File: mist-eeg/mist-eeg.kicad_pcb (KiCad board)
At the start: 4 copper layers, 50 x 75 mm, 233 parts, among them J1 Power_5V-14V, J10 J1310, J3 Audio, J4 Electrodes, J5 Micro_SD_Card_Det, J6 Extra GPIOs, J7 Digital buses, J8 J1312, J9 J1311, Q1 NMOS_DGS (3V3), Q2 NMOS_DGS (3.3V), Q3 NMOS_DGS (3.3V), Q4 PMOS_DGS (3.3V @ 1A), SW1 START, SW2 USER, SW3 SD_RST, SW4 RESET, SW5 ONOFF, U1 LTC2947, U10 ADAU1372, U11 ADS1299, U12 NX5427001Z, U5 TPS63070, U6 LT3042xMSE, U7 LT3042xMSE, U8 TPS63070, U9 TPS63070

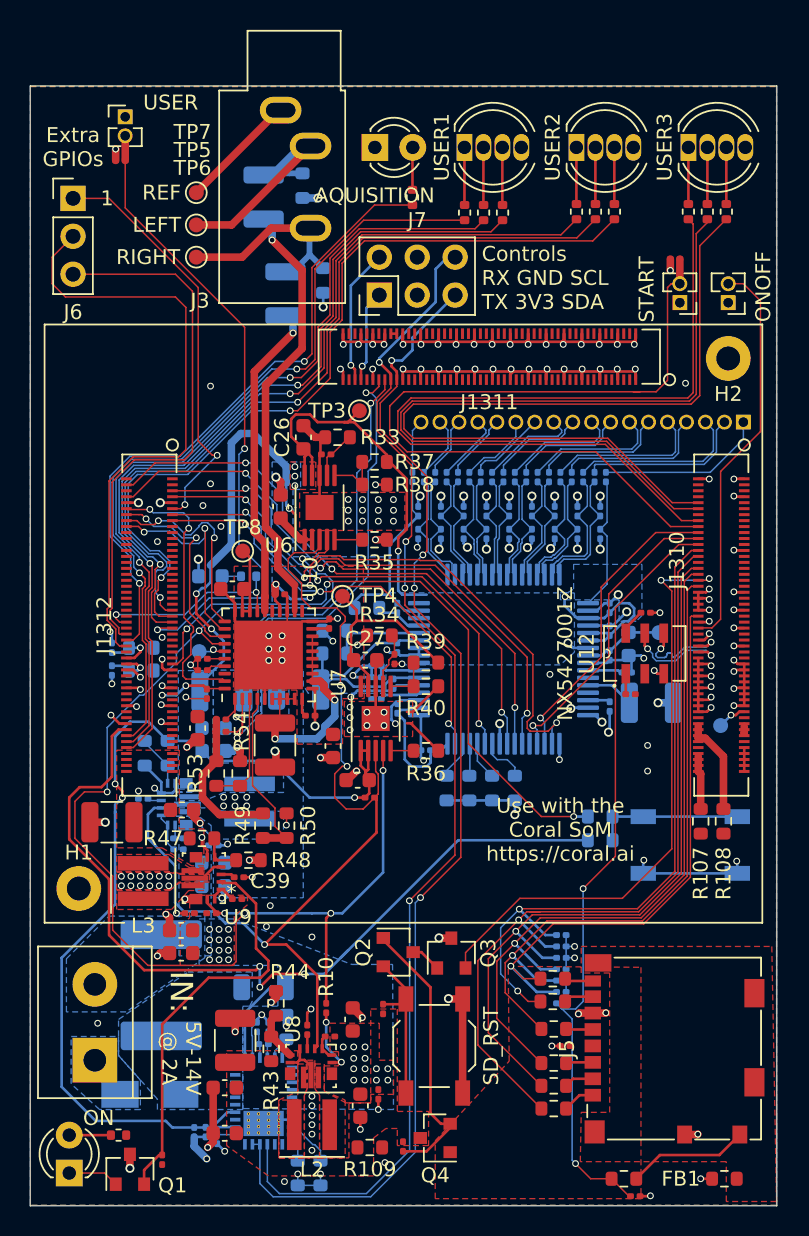
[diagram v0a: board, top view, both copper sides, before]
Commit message: Change buckboost regulator used
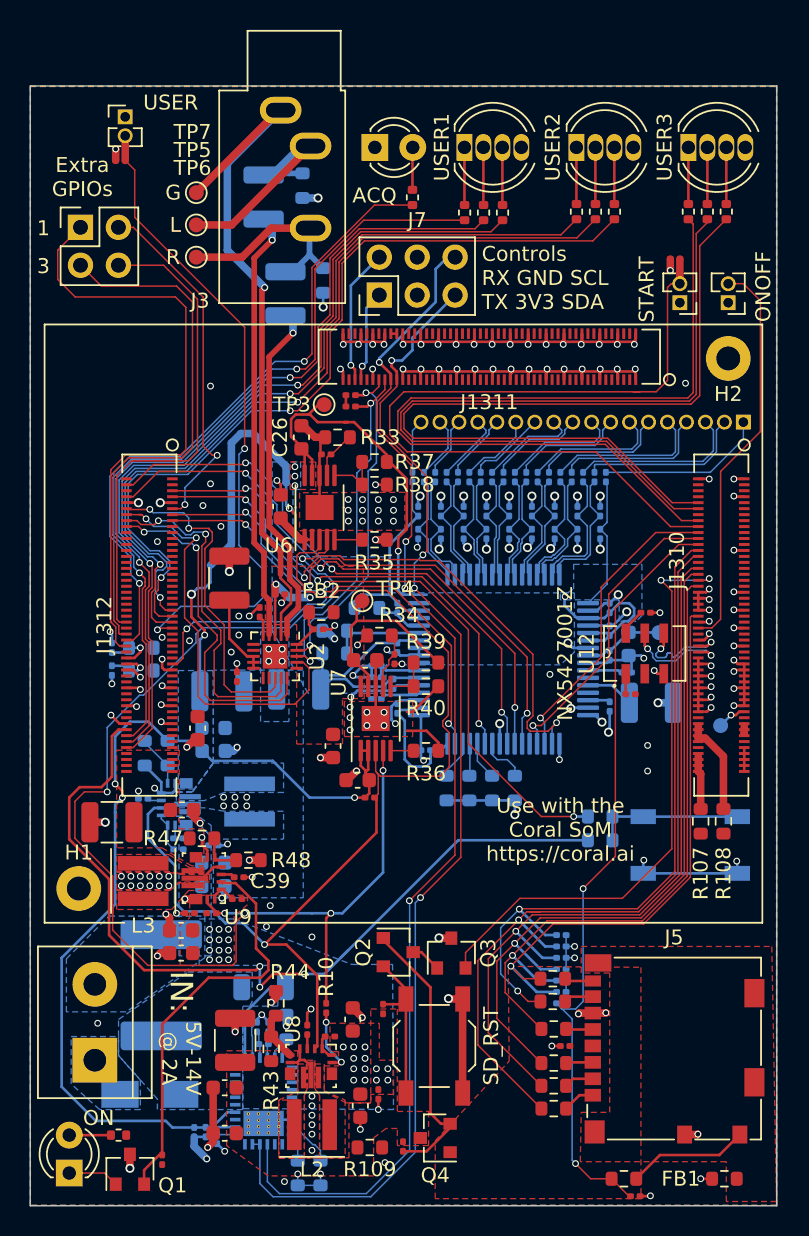
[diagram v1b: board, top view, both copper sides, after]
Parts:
- removed C53: 10uF, Capacitor_SMD:C_0603_1608Metric
- removed D4: AUDIO_ON, LED_SMD:LED_0603_1608Metric
- removed R49, R53: DNF, Resistor_SMD:R_0603_1608Metric
- removed R50, R54: 10k, Resistor_SMD:R_0603_1608Metric
- removed R55, R56: 4k7, Resistor_SMD:R_0201_0603Metric
- removed R57: 1k, Resistor_SMD:R_0402_1005Metric
- removed TP8: Reg, TestPoint:TestPoint_Pad_D1.0mm
- removed TP9: AUDIO_CLK, TestPoint:TestPoint_Pad_D1.0mm
- removed U10: ADAU1372, Package_DFN_QFN:QFN-40-1EP_6x6mm_P0.5mm_EP4.6x4.6mm
- added FB2: Ferrite_Bead_Small, Resistor_SMD:R_0603_1608Metric, F.Cu at (218.5, 69.2)
- added U2: SGTL5000XNLA3, Package_DFN_QFN:QFN-20-1EP_3x3mm_P0.4mm_EP1.65x1.65mm, F.Cu at (215.4, 72.2)
- D5: value AQUISITION -> ACQ
- J6: footprint Connector_PinHeader_2.54mm:PinHeader_1x03_P2.54mm_Vertical -> Connector_PinHeader_2.54mm:PinHeader_2x02_P2.54mm_Vertical
- R58, R59: value 2k -> 4k7
- TP5: value S -> T
- TP7: value T -> S
- moved R58 24.2 mm to (220.5, 54.7)
- moved R59 22.7 mm to (220.5, 55.5)
- moved C50 11.6 mm to (212.3, 67.0), turned to 90 degrees
- moved C51 5.81 mm to (218.3, 70.4)
- moved C52 4.72 mm to (214.4, 69.2)
- moved TP3 2.39 mm to (218.7, 55.3)
- moved C46 2.31 mm to (212.8, 73.6), turned to 90 degrees
- moved J6 2.00 mm to (202.4, 43.5)
- moved TP4 1.35 mm to (221.2, 68.5)
- moved C26 0.14 mm to (217.2, 57.5)
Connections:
- net /AUDIO_PWR_OK renamed /power/STAGE_2
- C51 pad 1: /+1V8_ANA -> /audio/DVDD
- C52 pad 1: /+1V8_ANA -> Net-(C52-Pad1)
- J3 pad S: GND -> /audio/HPGND
- J8 pad 11: /SoM/EXTRA_1 -> /SoM/EXTRA_2
- J8 pad 50: /~AUDIO_PWDN~ -> /SoM/EXTRA_4
- J8 pad 58: /SoM/EXTRA_2 -> /SoM/EXTRA_1
- TP7 pad 1: GND -> /audio/HPGND
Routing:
- net /audio/HPGND: track 0.00 -> 47.2 mm, vias 0 -> 1
- net /SoM/EXTRA_4: track 0.00 -> 32.9 mm
- net GND: track 298.6 -> 270.6 mm, vias 211 -> 207
- net /SoM/EXTRA_2: track 40.8 -> 23.9 mm, vias 0 -> 2
- net +3V3: track 26.6 -> 12.7 mm, vias 19 -> 21
- net /AUDIO_SDATA: track 13.6 -> 27.3 mm
- net /~AUDIO_PWDN~: track 13.4 -> 0.00 mm, vias 2 -> 0
- net /SoM/EXTRA_1: track 28.0 -> 41.1 mm, vias 2 -> 0
- net /AUDIO_SCL: track 36.1 -> 23.0 mm
- net /audio/ADDR0: track 12.0 -> 0.00 mm
- net /audio/CM: track 15.4 -> 5.48 mm, vias 2 -> 0
- net /AUDIO_LRCLK: track 13.6 -> 23.1 mm
- net /AUDIO_BCLK: track 14.0 -> 23.0 mm
- net /AUDIO_SDA: track 32.4 -> 24.0 mm
- net /audio/ADDR1: track 7.68 -> 0.00 mm
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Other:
- board text added: "3"
- board text added: "G"
- board text added: "L"
- board text added: "R"
- board text removed: "LEFT"
- board text removed: "REF"
- board text removed: "RIGHT"

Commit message: Switch to POL switching regulator to accelerate production of the board
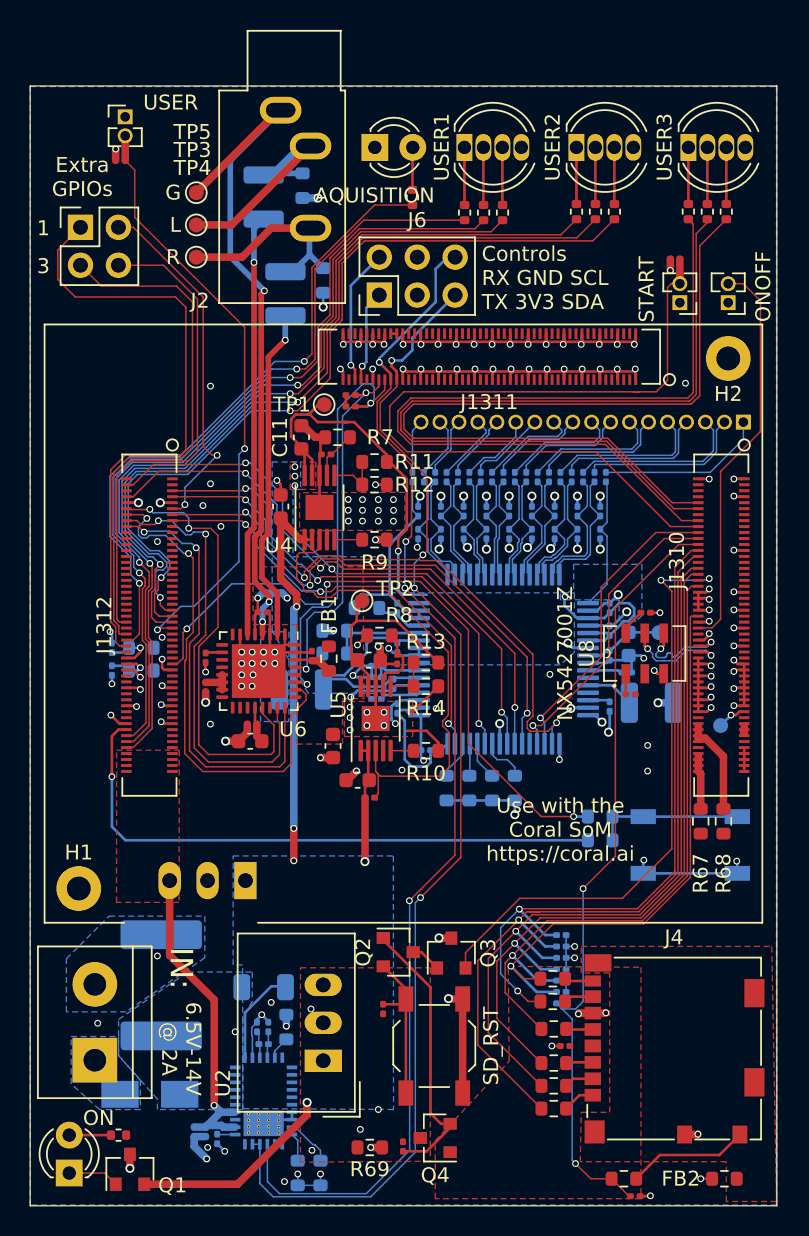
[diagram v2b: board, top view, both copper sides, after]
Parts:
- removed the C14 at (211.3, 86.0)
- removed the C16 at (211.3, 84.9)
- removed the C17 at (206.6, 81.7)
- removed the C18 at (211.3, 78.5)
- removed the C19 at (211.3, 77.0)
- removed the C20 at (211.8, 74.5)
- removed the C28 at (221.1, 102.3)
- removed the C29 at (220.6, 96.5)
- removed the C30 at (222.3, 101.5)
- removed the C31 at (217.6, 97.2)
- removed the C32 at (212.0, 101.1)
- removed the C33 at (212.0, 104.1)
- removed the C34 at (212.7, 97.9)
- removed the C36 at (209.1, 92.1)
- removed the C37 at (209.1, 90.6)
- removed the C38 at (209.7, 89.4)
- removed the C39 at (213.0, 87.0)
- removed the C40 at (209.2, 82.5)
- removed the C41 at (204.5, 83.3)
- removed the C50 at (212.3, 67.0)
- removed L1, L2, L3: 1u5H, Inductor_SMD:L_Coilcraft_XxL4040
- removed the R10 at (218.8, 95.8)
- removed the R29 at (208.9, 85.1)
- removed the R31 at (208.2, 78.7)
- removed the R32 at (206.7, 78.7)
- removed the R41 at (219.1, 97.7)
- removed the R44 at (215.5, 95.4)
- removed the R45 at (212.9, 88.5)
- removed the R47 at (210.5, 84.4)
- removed the R48 at (213.6, 85.9)
- removed the R5 at (211.1, 89.4)
- removed the R6 at (207.8, 105.9)
- removed R84: DNF, Resistor_SMD:R_0603_1608Metric
- removed the R9 at (208.9, 84.4)
- removed the U5 at (208.9, 82.1)
- removed the U8 at (217.8, 99.6)
- removed U9: TPS63070, mist-eeg:TPS630702RNMR
- added U3: TSR_2-2450, Converter_DCDC:Converter_DCDC_TRACO_TSR-1_THT, B.Cu at (213.4, 87.2)
- added U6: SGTL5000XNAA3, Package_DFN_QFN:QFN-32-1EP_5x5mm_P0.5mm_EP3.6x3.6mm, F.Cu at (214.3, 73.2)
- C15: value 10uF -> 0u1F; footprint Capacitor_SMD:C_0603_1608Metric -> Capacitor_SMD:C_0201_0603Metric; moved to F.Cu
- D3: renamed from D5; value ACQ -> AQUISITION
- J1: value Power_5V-14V -> Power_6.5V-14V
- J4: renamed from J5; value Micro_SD_Card_Det -> Molex 104031
- R43: value 31k3 -> DNF; moved to B.Cu
- U2: value SGTL5000XNLA3 -> TSR_1-2433; footprint Package_DFN_QFN:QFN-20-1EP_3x3mm_P0.4mm_EP1.65x1.65mm -> Converter_DCDC:Converter_DCDC_TRACO_TSR-1_THT
- moved R43 28.3 mm to (219.4, 70.5), turned to 180 degrees
- moved U2 27.3 mm to (218.6, 99.3), turned to 90 degrees
- moved C15 13.3 mm to (210.7, 74.3), turned to 270 degrees
- moved C16 4.73 mm to (210.7, 72.3), turned to 270 degrees
- moved C18 3.63 mm to (213.7, 77.9), turned to 180 degrees
- moved C17 3.33 mm to (213.9, 76.7), turned to 180 degrees
- moved FB1 3.15 mm to (219.0, 72.4), turned to 90 degrees
- moved G*** 2.70 mm to (227.6, 97.6)
- moved C20 1.83 mm to (217.9, 72.2), turned to 90 degrees
- moved C21 1.67 mm to (214.6, 69.2)
- moved C12 0.23 mm to (221.7, 72.5)
- moved C10 0.18 mm to (223.6, 72.4)
- moved C26 0.18 mm to (217.2, 74.4)
- renumbered C25 to C10, C26 to C11, C27 to C12, C44 to C13, C45 to C14, C52 to C16, C46 to C17, C47 to C18, C48 to C19, C51 to C20, C49 to C21, C54 to C22, C55 to C23, C56 to C24, C57 to C25, C58 to C26, C59 to C27, C60 to C28, C61 to C29, C62 to C30, C63 to C31, C64 to C32, C65 to C33, C66 to C34, C67 to C35, C68 to C36, C69 to C37, C70 to C38, C71 to C39, C72 to C40, C73 to C41, C74 to C42, C75 to C43, C76 to C44, C77 to C45, C78 to C46, C79 to C47, C80 to C48, C81 to C49, C82 to C50, C83 to C51, C84 to C52, C85 to C53, C86 to C54, C87 to C55, C88 to C56, C22 to C7, C23 to C8, C24 to C9, D12 to D10, D13 to D11, D14 to D12, D15 to D13, D6 to D4, D7 to D5, D8 to D6, D9 to D7, D10 to D8, D11 to D9, FB2 to FB1, FB1 to FB2, J3 to J2, J4 to J3, J6 to J5, J7 to J6, J8 to J7, J9 to J8, J10 to J9, R36 to R10, R37 to R11, R38 to R12, R39 to R13, R40 to R14, R51 to R15, R52 to R16, R58 to R17, R59 to R18, R60 to R19, R8 to R2, R61 to R20, R62 to R21, R63 to R22, R64 to R23, R65 to R24, R66 to R25, R67 to R26, R68 to R27, R69 to R28, R70 to R29, R2 to R3, R71 to R30, R72 to R31, R73 to R32, R74 to R33, R75 to R34, R76 to R35, R77 to R36, R78 to R37, R79 to R38, R80 to R39, R3 to R4, R81 to R40, R82 to R41, R83 to R42, R85 to R44, R86 to R45, R87 to R46, R88 to R47, R89 to R48, R90 to R49, R4 to R5, R91 to R50, R92 to R51, R93 to R52, R94 to R53, R95 to R54, R96 to R55, R97 to R56, R98 to R57, R99 to R58, R100 to R59, R7 to R6, R101 to R60, R102 to R61, R103 to R62, R104 to R63, R105 to R64, R11 to R65, R106 to R66, R107 to R67, R108 to R68, R109 to R69, R33 to R7, R110 to R70, R111 to R71, R112 to R72, R113 to R73, R114 to R74, R115 to R75, R116 to R76, R34 to R8, R35 to R9, TP3 to TP1, TP4 to TP2, TP5 to TP3, TP6 to TP4, TP7 to TP5, TP10 to TP6, TP11 to TP7, U6 to U4, U7 to U5, U11 to U7, U12 to U8
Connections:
- net /power/STAGE_1 renamed /power/audio-power/ENA
- C1 pad 1: /power/+5V25 -> /+5V_SOM
- C15 pad 1: /power/+PWR -> /audio/CM
- C16 pad 1: Net-(C52-Pad1) -> Net-(C16-Pad1)
- C2 pad 1: /power/+5V25 -> /+5V_SOM
- C7 pad 1: /power/+5V25 -> /power/+PWR
- C8 pad 1: /power/+5V25 -> /power/+PWR
- Q1 pad 2: /power/PG -> /power/+PWR
- R43 pad 1: /+3V3_SD -> /EEG/BIASREF
- R43 pad 2: /power/SD-power/FB -> GND
- R5 pad 2: /power/+5V25 -> /power/+PWR
- U1 pad 18: /power/+5V25 -> /+5V_SOM
- U1 pad 20: /power/+5V25 -> /+5V_SOM
- U2 pad 1: /audio/RIGHT -> /power/+PWR
- U2 pad 2: /audio/HPGND -> GND
- U2 pad 3: /+1V8_ANA -> /+3V3_SD
- U4 pad 1: /power/+5V25 -> /power/+PWR
- U4 pad 2: /power/+5V25 -> /power/+PWR
- U4 pad 4: /power/STAGE_2 -> (no net)
- U5 pad 1: /power/+5V25 -> /power/+PWR
- U5 pad 2: /power/+5V25 -> /power/+PWR
- U5 pad 4: /power/STAGE_2 -> (no net)
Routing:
- net /power/+5V25: track 96.5 -> 0.00 mm, vias 6 -> 0
- net /power/STAGE_2: track 82.8 -> 0.00 mm, vias 6 -> 0
- net /power/+PWR: track 7.20 -> 54.5 mm, vias 26 -> 5
- net /power/audio-power/ENA: track 70.5 -> 33.5 mm, vias 1 -> 0
- net /power/PG: track 27.7 -> 0.00 mm
- net /+5V_SOM: track 0.00 -> 22.2 mm, vias 0 -> 1
- net /SoM/~PWR_ON~: track 56.9 -> 39.5 mm, vias 3 -> 1
- net GND: track 270.6 -> 256.3 mm, vias 207 -> 176
- net /AUDIO_MCLK: track 22.2 -> 30.5 mm
- net /AUDIO_LRCLK: track 23.1 -> 30.2 mm
- net /AUDIO_BCLK: track 23.0 -> 30.0 mm
- net /AUDIO_SDATA: track 27.3 -> 34.3 mm
- net /AUDIO_SDA: track 24.0 -> 28.6 mm
- net /power/SD-power/ENA: track 4.36 -> 0.00 mm, vias 2 -> 0
- net /USER: track 44.2 -> 40.4 mm
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- removed copper zone on B.Cu, net /power/+5V25
- removed copper zone on F.Cu, net /power/+PWR
- removed copper zone on B.Cu, net Net-(L1-Pad1)
- removed copper zone on B.Cu, net Net-(L1-Pad2)
- removed copper zone on F.Cu, net Net-(L2-Pad1)
- removed copper zone on F.Cu, net Net-(L2-Pad2)
- removed copper zone on F.Cu, net Net-(L3-Pad1)
- removed copper zone on F.Cu, net Net-(L3-Pad2)
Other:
- board text added: "6.5V-14V @ 2A"
- board text added: "Portiloop rev. 1D"
- board text removed: "5V-14V @ 2A"
- board text removed: "Portiloop rev. 1B"

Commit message: Add BoM
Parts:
- C26: value 47uF -> 100uF
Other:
- rule trace_min: 0.1016 -> 0.1
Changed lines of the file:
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@@
   )
   (layers
-    (0 F.Cu signal hide)
+    (0 F.Cu signal)
     (1 In1.Cu signal hide)
     (2 In2.Cu signal hide)
-    (31 B.Cu signal hide)
+    (31 B.Cu signal)
     (32 B.Adhes user hide)
     (33 F.Adhes user hide)
@@
     (zone_clearance 0.1016)
     (zone_45_only no)
-    (trace_min 0.1016)
+    (trace_min 0.1)
     (via_size 0.4572)
     (via_drill 0.3048)
@@
       (effects (font (size 0.381 0.381) (thickness 0.0762)))
     )
+    (fp_line (start -2.3 2) (end 8.4 2) (layer F.Fab) (width 0.1))
+    (fp_line (start -3.42 2.12) (end -3.42 -5.73) (layer F.SilkS) (width 0.12))
+    (fp_line (start -3.42 -5.73) (end 8.52 -5.73) (layer F.SilkS) (width 0.12))
+    (fp_line (start 8.52 -5.73) (end 8.52 2.12) (layer F.SilkS) (width 0.12))
+    (fp_line (start 8.52 2.12) (end -3.42 2.12) (layer F.SilkS) (width 0.12))
+    (fp_line (start -3.55 -5.85) (end 8.65 -5.85) (layer F.CrtYd) (width 0.05))
+    (fp_line (start 8.65 -5.85) (end 8.65 2.25) (layer F.CrtYd) (width 0.05))
+    (fp_line (start 8.65 2.25) (end -3.55 2.25) (layer F.CrtYd) (width 0.05))
+    (fp_line (start -3.55 2.25) (end -3.55 -5.85) (layer F.CrtYd) (width 0.05))
+    (fp_line (start -3.3 -5.6) (end 8.4 -5.6) (layer F.Fab) (width 0.1))
+    (fp_line (start 8.4 2) (end 8.4 -5.6) (layer F.Fab) (width 0.1))
+    (fp_line (start -3.3 1) (end -3.3 -5.6) (layer F.Fab) (width 0.1))
+    (fp_line (start -3.3 1) (end -2.3 2) (layer F.Fab) (width 0.1))
+    (fp_line (start -3.75 0) (end -3.75 2.45) (layer F.SilkS) (width 0.12))
+    (fp_line (start -3.75 2.45) (end -1.42 2.45) (layer F.SilkS) (width 0.12))
     (fp_text user %R (at 2.8915 -1.8325 180) (layer F.Fab)
       (effects (font (size 1 1) (thickness 0.15)))
     )
-    (fp_line (start -3.75 2.45) (end -1.42 2.45) (layer F.SilkS) (width 0.12))
-    (fp_line (start -3.75 0) (end -3.75 2.45) (layer F.SilkS) (width 0.12))
-    (fp_line (start -3.3 1) (end -2.3 2) (layer F.Fab) (width 0.1))
-    (fp_line (start -3.3 1) (end -3.3 -5.6) (layer F.Fab) (width 0.1))
-    (fp_line (start 8.4 2) (end 8.4 -5.6) (layer F.Fab) (width 0.1))
-    (fp_line (start -3.3 -5.6) (end 8.4 -5.6) (layer F.Fab) (width 0.1))
-    (fp_line (start -3.55 2.25) (end -3.55 -5.85) (layer F.CrtYd) (width 0.05))
-    (fp_line (start 8.65 2.25) (end -3.55 2.25) (layer F.CrtYd) (width 0.05))
-    (fp_line (start 8.65 -5.85) (end 8.65 2.25) (layer F.CrtYd) (width 0.05))
-    (fp_line (start -3.55 -5.85) (end 8.65 -5.85) (layer F.CrtYd) (width 0.05))
-    (fp_line (start 8.52 2.12) (end -3.42 2.12) (layer F.SilkS) (width 0.12))
-    (fp_line (start 8.52 -5.73) (end 8.52 2.12) (layer F.SilkS) (width 0.12))
-    (fp_line (start -3.42 -5.73) (end 8.52 -5.73) (layer F.SilkS) (width 0.12))
-    (fp_line (start -3.42 2.12) (end -3.42 -5.73) (layer F.SilkS) (width 0.12))
-    (fp_line (start -2.3 2) (end 8.4 2) (layer F.Fab) (width 0.1))
+    (pad 1 thru_hole rect (at 0 0 90) (size 1.5 2.5) (drill 1) (layers *.Cu *.Mask)
+      (net 13 /power/+PWR))
+    (pad 2 thru_hole oval (at 2.54 0 90) (size 1.5 2.5) (drill 1) (layers *.Cu *.Mask)
+      (net 1 GND))
     (pad 3 thru_hole oval (at 5.08 0 90) (size 1.5 2.5) (drill 1) (layers *.Cu *.Mask)
       (net 125 /+3V3_SD))
-    (pad 2 thru_hole oval (at 2.54 0 90) (size 1.5 2.5) (drill 1) (layers *.Cu *.Mask)
-      (net 1 GND))
-    (pad 1 thru_hole rect (at 0 0 90) (size 1.5 2.5) (drill 1) (layers *.Cu *.Mask)
-      (net 13 /power/+PWR))
     (model ${KISYS3DMOD}/Converter_DCDC.3dshapes/Converter_DCDC_TRACO_TSR-1_THT.wrl
       (at (xyz 0 0 0))
@@
       (effects (font (size 1 1) (thickness 0.15)) (justify mirror))
     )
-    (fp_text value 47uF (at 0 -2.032) (layer B.Fab)
+    (fp_text value 100uF (at 0 -2.032) (layer B.Fab)
       (effects (font (size 0.381 0.381) (thickness 0.0762)) (justify mirror))
     )
-    (fp_line (start 2.3 -1.6) (end -2.3 -1.6) (layer B.CrtYd) (width 0.05))
-    (fp_line (start 2.3 1.6) (end 2.3 -1.6) (layer B.CrtYd) (width 0.05))
-    (fp_line (start -2.3 1.6) (end 2.3 1.6) (layer B.CrtYd) (width 0.05))
-    (fp_line (start -2.3 -1.6) (end -2.3 1.6) (layer B.CrtYd) (width 0.05))
-    (fp_line (start -0.711252 -1.36) (end 0.711252 -1.36) (layer B.SilkS) (width 0.12))
-    (fp_line (start -0.711252 1.36) (end 0.711252 1.36) (layer B.SilkS) (width 0.12))
-    (fp_line (start 1.6 -1.25) (end -1.6 -1.25) (layer B.Fab) (width 0.1))
-    (fp_line (start 1.6 1.25) (end 1.6 -1.25) (layer B.Fab) (width 0.1))
-    (fp_line (start -1.6 1.25) (end 1.6 1.25) (layer B.Fab) (width 0.1))
-    (fp_line (start -1.6 -1.25) (end -1.6 1.25) (layer B.Fab) (width 0.1))
     (fp_text user %R (at 0 0) (layer B.Fab)
       (effects (font (size 0.8 0.8) (thickness 0.12)) (justify mirror))
     )
-    (pad 2 smd roundrect (at 1.475 0 180) (size 1.15 2.7) (layers B.Cu B.Paste B.Mask) (roundrect_rratio 0.2173904347826087)
-      (net 1 GND))
+    (fp_line (start -1.6 -1.25) (end -1.6 1.25) (layer B.Fab) (width 0.1))
+    (fp_line (start -1.6 1.25) (end 1.6 1.25) (layer B.Fab) (width 0.1))
+    (fp_line (start 1.6 1.25) (end 1.6 -1.25) (layer B.Fab) (width 0.1))
+    (fp_line (start 1.6 -1.25) (end -1.6 -1.25) (layer B.Fab) (width 0.1))
+    (fp_line (start -0.711252 1.36) (end 0.711252 1.36) (layer B.SilkS) (width 0.12))
+    (fp_line (start -0.711252 -1.36) (end 0.711252 -1.36) (layer B.SilkS) (width 0.12))
+    (fp_line (start -2.3 -1.6) (end -2.3 1.6) (layer B.CrtYd) (width 0.05))
+    (fp_line (start -2.3 1.6) (end 2.3 1.6) (layer B.CrtYd) (width 0.05))
+    (fp_line (start 2.3 1.6) (end 2.3 -1.6) (layer B.CrtYd) (width 0.05))
+    (fp_line (start 2.3 -1.6) (end -2.3 -1.6) (layer B.CrtYd) (width 0.05))
     (pad 1 smd roundrect (at -1.475 0 180) (size 1.15 2.7) (layers B.Cu B.Paste B.Mask) (roundrect_rratio 0.2173904347826087)
       (net 6 /+5V0_ANA))
+    (pad 2 smd roundrect (at 1.475 0 180) (size 1.15 2.7) (layers B.Cu B.Paste B.Mask) (roundrect_rratio 0.2173904347826087)
+      (net 1 GND))
     (model ${KISYS3DMOD}/Capacitor_SMD.3dshapes/C_1210_3225Metric.wrl
       (at (xyz 0 0 0))
@@
       (effects (font (size 0.8 0.8) (thickness 0.12)) (justify mirror))
     )
-    (pad 2 smd roundrect (at 1.4625 0 180) (size 1.125 1.75) (layers B.Cu B.Paste B.Mask) (roundrect_rratio 0.2222204444444444)
+    (pad 2 smd roundrect (at 1.4625 0 180) (size 1.125 1.75) (layers B.Cu B.Paste B.Mask) (roundrect_rratio 0.2222195555555556)
       (net 12 /power/+PWR_IN))
-    (pad 1 smd roundrect (at -1.4625 0 180) (size 1.125 1.75) (layers B.Cu B.Paste B.Mask) (roundrect_rratio 0.2222204444444444)
+    (pad 1 smd roundrect (at -1.4625 0 180) (size 1.125 1.75) (layers B.Cu B.Paste B.Mask) (roundrect_rratio 0.2222195555555556)
       (net 13 /power/+PWR))
     (model ${KISYS3DMOD}/Resistor_SMD.3dshapes/R_1206_3216Metric.wrl
